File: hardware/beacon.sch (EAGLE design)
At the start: 13 parts, among them IC1 LM1117SX-3.3, IC2 FT232RL, X1 MINI-USB-UX60A-MB-5ST

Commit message: update schematic
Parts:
- added C5: 100n, rcl:C-EUC1206K
- added Q1, Q2: BC850SMD, transistor-npn:BC850SMD
- added R10, R4, R5, R6, R7, R8, R9: 10k, rcl:R-EU_R1206
- added RESET: (no value), switch-omron:10-XX
- added SV1: (no value), con-lstb:MA06-1
- added SV2: HC-SR04, con-lstb:MA04-1
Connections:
- new net DTR: IC2.!DTR, Q2.E, R4.1, SV1.6
- new net ECHO: SV2.2, U1.GPIO12
- new net GPIO0: Q2.C, R9.2, U1.GPIO0
- new net N$11: Q2.B, R5.2
- new net N$12: R10.2, U1.GPIO2
- new net N$6: R6.1, U1.GPIO15
- new net N$8: R7.2, U1.CH_PD
- new net N$9: Q1.B, R4.2
- new net RST: Q1.C, R8.2, RESET.S, RESET.S1, U1.RESET
- new net RTS: IC2.!RTS, Q1.E, R5.1
- new net TRIGGER: SV2.3, U1.GPIO13
- net +3V3: now also C5.1, R10.1, R7.1, R8.1, R9.1, SV1.3
- net +5V: now also SV2.4
- net GND: now also C5.2, R6.2, RESET.P, RESET.P1, SV1.1, SV2.1
- net RX: now also SV1.5
- net TX: now also SV1.4
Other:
- moved on the sheet: U1

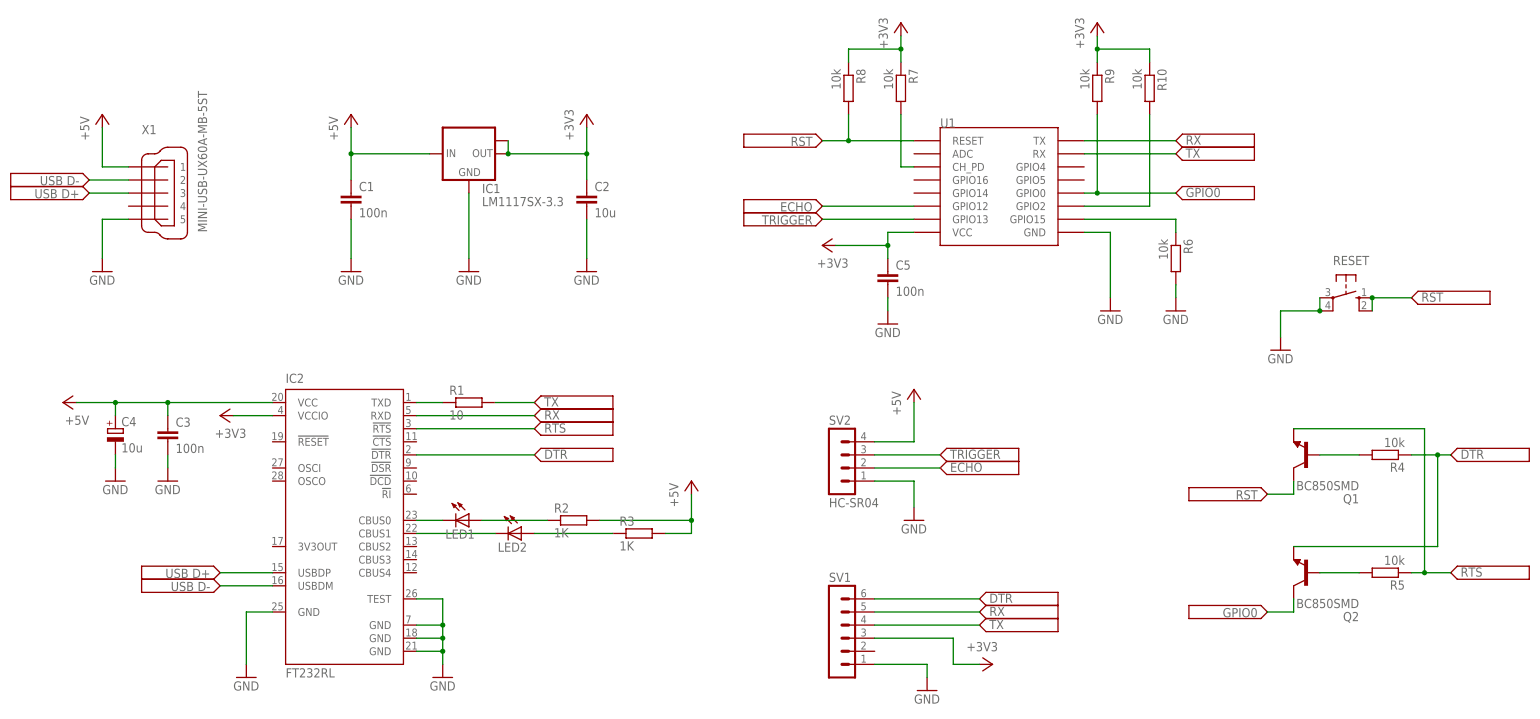
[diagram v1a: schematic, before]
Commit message: update schematic, change ft232 to ch340g
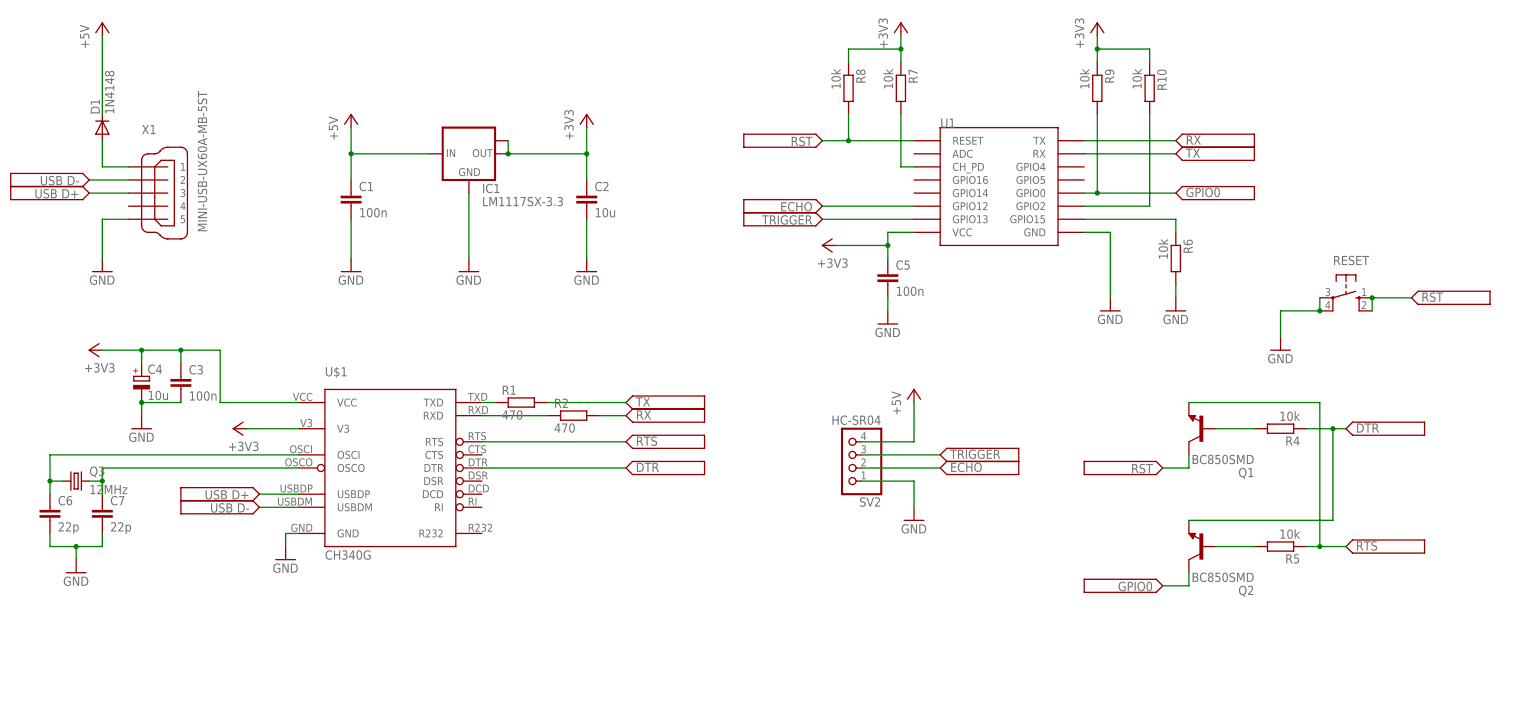
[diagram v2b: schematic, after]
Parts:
- removed IC2: FT232RL, ftdichip:FT232RL
- removed LED1, LED2: (no value), led:LEDSMT1206
- removed R3: 1K, rcl:R-EU_R1206
- removed SV1: (no value), con-lstb:MA06-1
- added C6, C7: 22p, rcl:C-EUC1206K
- added D1: 1N4148, diode:S1M
- added Q3: 12MHz, crystal:CRYSTALSM49
- added U$1: CH340G, ch340g:CH340G
- R1: value 10 -> 470
- R2: value 1K -> 470
- SV2: device con-lstb:MA04-1 -> pinhead:PINHD-1X4/90
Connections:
- net +3V3: now also C3.1, C4.+, U$1.V3, U$1.VCC; no longer IC2.VCCIO, SV1.3
- net +5V: now also D1.C; no longer C3.1, C4.+, IC2.VCC, R2.2, R3.2, X1.1
- net DTR: now also U$1.DTR; no longer IC2.!DTR, SV1.6
- net GND: now also C6.2, C7.2, U$1.GND; no longer IC2.GND, IC2.GND@1, IC2.GND@2, IC2.GND@A, IC2.TEST, SV1.1
- net N$1: now also R1.1, U$1.TXD; no longer IC2.CBUS0, LED1.C
- net N$2: now also R2.1, U$1.RXD; no longer IC2.CBUS1, LED2.C
- net N$3: now also C6.1, Q3.1, U$1.OSCI; no longer IC2.TXD, R1.1
- net N$4: now also C7.1, Q3.2, U$1.OSCO; no longer LED1.A, R2.1
- net N$5: now also D1.A, X1.1; no longer LED2.A, R3.1
- net RTS: now also U$1.RTS; no longer IC2.!RTS
- net RX: now also R2.2; no longer IC2.RXD, SV1.5
- net TX: no longer SV1.4
- net USBDM: now also U$1.USBDM; no longer IC2.USBDM
- net USBDP: now also U$1.USBDP; no longer IC2.USBDP
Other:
- moved on the sheet: C3, C4, Q1, Q2, R1, R2, R4, R5

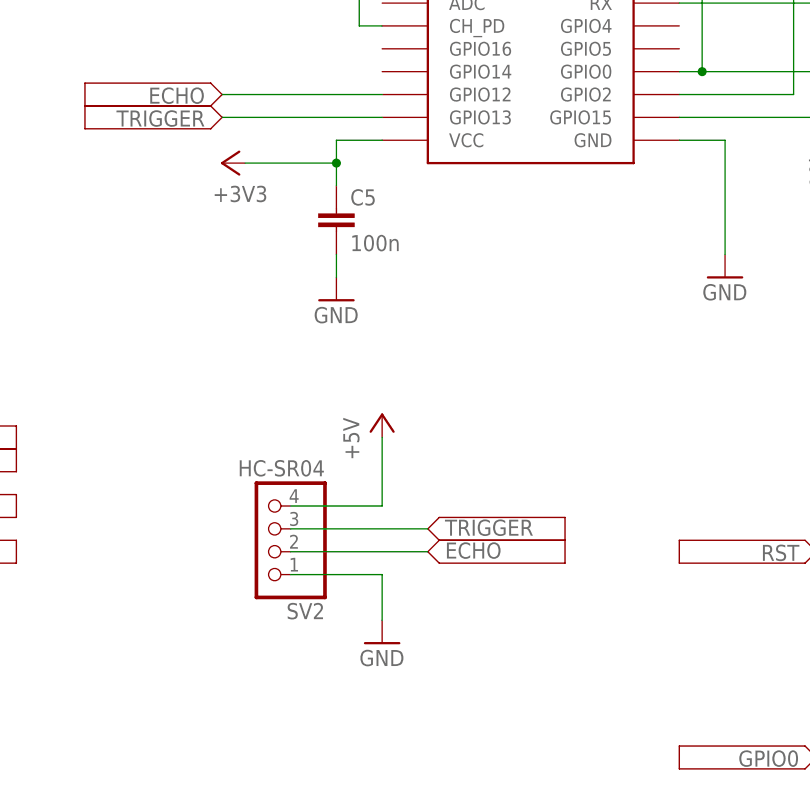
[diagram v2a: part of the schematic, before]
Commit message: create board, update ch340g lbr
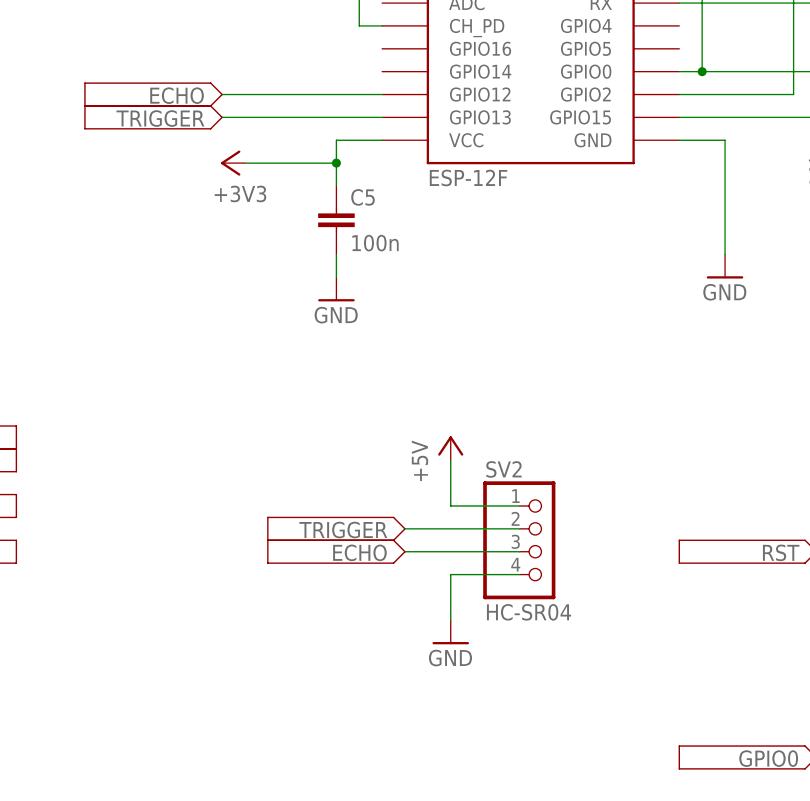
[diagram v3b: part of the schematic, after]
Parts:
- U1: value (none) -> ESP-12F
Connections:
- net +5V: now also SV2.1; no longer SV2.4
- net ECHO: now also SV2.3; no longer SV2.2
- net GND: now also SV2.4; no longer SV2.1
- net TRIGGER: now also SV2.2; no longer SV2.3
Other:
- moved on the sheet: SV2
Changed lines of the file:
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@@
 <parts>
 <part name="X1" library="con-hirose" deviceset="MINI-USB-" device="UX60A-MB-5ST"/>
-<part name="U1" library="esp8266modules" deviceset="ESP12" device="SMD"/>
+<part name="U1" library="esp8266modules" deviceset="ESP12" device="SMD" value="ESP-12F"/>
 <part name="IC1" library="lm1117" deviceset="LM1117SX-*" device="" technology="3.3"/>
 <part name="C1" library="rcl" deviceset="C-EU" device="C1206K" value="100n"/>
@@
 <instance part="GND13" gate="1" x="185.42" y="43.18"/>
 <instance part="+3V7" gate="G$1" x="170.18" y="99.06"/>
-<instance part="SV2" gate="A" x="121.92" y="15.24" rot="R180"/>
-<instance part="TRIGGER" gate="G$1" x="154.94" y="15.24"/>
-<instance part="ECHO" gate="G$1" x="154.94" y="12.7"/>
-<instance part="GND14" gate="1" x="134.62" y="2.54"/>
-<instance part="P+5" gate="1" x="134.62" y="27.94"/>
+<instance part="SV2" gate="A" x="152.4" y="12.7"/>
+<instance part="TRIGGER" gate="G$1" x="121.92" y="15.24" rot="R180"/>
+<instance part="ECHO" gate="G$1" x="121.92" y="12.7" rot="R180"/>
+<instance part="GND14" gate="1" x="142.24" y="2.54"/>
+<instance part="P+5" gate="1" x="142.24" y="25.4"/>
 <instance part="TRIGGER1" gate="G$1" x="101.6" y="60.96" rot="R180"/>
 <instance part="ECHO1" gate="G$1" x="101.6" y="63.5" rot="R180"/>
@@
 </segment>
 <segment>
-<pinref part="SV2" gate="A" pin="1"/>
-<pinref part="GND14" gate="1" pin="GND"/>
-<wire x1="124.46" y1="10.16" x2="134.62" y2="10.16" width="0.1524" layer="91"/>
-<wire x1="134.62" y1="10.16" x2="134.62" y2="5.08" width="0.1524" layer="91"/>
-</segment>
-<segment>
 <pinref part="R6" gate="G$1" pin="2"/>
 <pinref part="GND13" gate="1" pin="GND"/>
@@
 <wire x1="15.24" y1="0" x2="12.7" y2="0" width="0.1524" layer="91"/>
 <wire x1="12.7" y1="0" x2="12.7" y2="-2.54" width="0.1524" layer="91"/>
+</segment>
+<segment>
+<pinref part="SV2" gate="A" pin="4"/>
+<pinref part="GND14" gate="1" pin="GND"/>
+<wire x1="149.86" y1="10.16" x2="142.24" y2="10.16" width="0.1524" layer="91"/>
+<wire x1="142.24" y1="10.16" x2="142.24" y2="5.08" width="0.1524" layer="91"/>
 </segment>
 </net>
@@
 </segment>
 <segment>
-<pinref part="P+5" gate="1" pin="+5V"/>
-<pinref part="SV2" gate="A" pin="4"/>
-<wire x1="134.62" y1="25.4" x2="134.62" y2="17.78" width="0.1524" layer="91"/>
-<wire x1="134.62" y1="17.78" x2="124.46" y2="17.78" width="0.1524" layer="91"/>
-</segment>
-<segment>
 <pinref part="D1" gate="G$1" pin="C"/>
 <pinref part="P+2" gate="1" pin="+5V"/>
 <wire x1="-22.86" y1="81.28" x2="-22.86" y2="96.52" width="0.1524" layer="91"/>
 </segment>
+<segment>
+<pinref part="SV2" gate="A" pin="1"/>
+<pinref part="P+5" gate="1" pin="+5V"/>
+<wire x1="149.86" y1="17.78" x2="142.24" y2="17.78" width="0.1524" layer="91"/>
+<wire x1="142.24" y1="17.78" x2="142.24" y2="22.86" width="0.1524" layer="91"/>
+</segment>
 </net>
 <net name="USBDP" class="0">
@@
 <net name="TRIGGER" class="0">
 <segment>
-<pinref part="SV2" gate="A" pin="3"/>
-<wire x1="139.7" y1="15.24" x2="124.46" y2="15.24" width="0.1524" layer="91"/>
-</segment>
-<segment>
 <pinref part="U1" gate="G$1" pin="GPIO13"/>
 <wire x1="134.62" y1="60.96" x2="116.84" y2="60.96" width="0.1524" layer="91"/>
 </segment>
+<segment>
+<pinref part="SV2" gate="A" pin="2"/>
+<wire x1="149.86" y1="15.24" x2="137.16" y2="15.24" width="0.1524" layer="91"/>
+</segment>
 </net>
 <net name="ECHO" class="0">
-<segment>
-<pinref part="SV2" gate="A" pin="2"/>
-<wire x1="139.7" y1="12.7" x2="124.46" y2="12.7" width="0.1524" layer="91"/>
-</segment>
 <segment>
 <pinref part="U1" gate="G$1" pin="GPIO12"/>
 <wire x1="134.62" y1="63.5" x2="116.84" y2="63.5" width="0.1524" layer="91"/>
+</segment>
+<segment>
+<pinref part="SV2" gate="A" pin="3"/>
+<wire x1="149.86" y1="12.7" x2="137.16" y2="12.7" width="0.1524" layer="91"/>
 </segment>
 </net>
@@
 </sheet>
 </sheets>
+<errors>
+</errors>
 </schematic>
 </drawing>

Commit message: add test pads
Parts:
- added TP1, TP2, TP3, TP4: TPSQTP20SQ, testpad:TPSQTP20SQ
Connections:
- net +3V3: now also TP4.TP
- net GND: now also TP1.TP
- net RX: now also TP3.TP
- net TX: now also TP2.TP
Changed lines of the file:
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@@
 <part name="GND8" library="supply1" deviceset="GND" device=""/>
 <part name="D1" library="diode" deviceset="S1M" device="" value="1N4148"/>
+<part name="TP1" library="testpad" deviceset="TPSQ" device="TP20SQ"/>
+<part name="TP2" library="testpad" deviceset="TPSQ" device="TP20SQ"/>
+<part name="TP3" library="testpad" deviceset="TPSQ" device="TP20SQ"/>
+<part name="GND9" library="supply1" deviceset="GND" device=""/>
+<part name="TX2" library="supply2" deviceset="V&lt;--" device="" value="TX"/>
+<part name="RX2" library="supply2" deviceset="V&lt;--" device="" value="RX"/>
+<part name="TP4" library="testpad" deviceset="TPSQ" device="TP20SQ"/>
+<part name="+3V4" library="supply1" deviceset="+3V3" device=""/>
 </parts>
 <sheets>
@@
 <instance part="GND8" gate="1" x="-27.94" y="-7.62"/>
 <instance part="D1" gate="G$1" x="-22.86" y="78.74" rot="R90"/>
+<instance part="TP1" gate="G$1" x="220.98" y="66.04" rot="R270"/>
+<instance part="TP2" gate="G$1" x="220.98" y="71.12" rot="R270"/>
+<instance part="TP3" gate="G$1" x="220.98" y="76.2" rot="R270"/>
+<instance part="GND9" gate="1" x="228.6" y="60.96"/>
+<instance part="TX2" gate="G$1" x="248.92" y="71.12"/>
+<instance part="RX2" gate="G$1" x="248.92" y="76.2"/>
+<instance part="TP4" gate="G$1" x="220.98" y="81.28" rot="R270"/>
+<instance part="+3V4" gate="G$1" x="228.6" y="88.9"/>
 </instances>
 <busses>
@@
 <wire x1="149.86" y1="10.16" x2="142.24" y2="10.16" width="0.1524" layer="91"/>
 <wire x1="142.24" y1="10.16" x2="142.24" y2="5.08" width="0.1524" layer="91"/>
+</segment>
+<segment>
+<pinref part="TP1" gate="G$1" pin="TP"/>
+<pinref part="GND9" gate="1" pin="GND"/>
+<wire x1="223.52" y1="66.04" x2="228.6" y2="66.04" width="0.1524" layer="91"/>
+<wire x1="228.6" y1="66.04" x2="228.6" y2="63.5" width="0.1524" layer="91"/>
 </segment>
 </net>
@@
 <wire x1="0" y1="25.4" x2="0" y2="35.56" width="0.1524" layer="91"/>
 </segment>
+<segment>
+<pinref part="TP4" gate="G$1" pin="TP"/>
+<pinref part="+3V4" gate="G$1" pin="+3V3"/>
+<wire x1="223.52" y1="81.28" x2="228.6" y2="81.28" width="0.1524" layer="91"/>
+<wire x1="228.6" y1="81.28" x2="228.6" y2="86.36" width="0.1524" layer="91"/>
+</segment>
 </net>
 <net name="+5V" class="0">
@@
 <wire x1="73.66" y1="22.86" x2="78.74" y2="22.86" width="0.1524" layer="91"/>
 </segment>
+<segment>
+<pinref part="TP3" gate="G$1" pin="TP"/>
+<wire x1="223.52" y1="76.2" x2="233.68" y2="76.2" width="0.1524" layer="91"/>
+</segment>
 </net>
 <net name="TX" class="0">
@@
 <wire x1="63.5" y1="25.4" x2="78.74" y2="25.4" width="0.1524" layer="91"/>
 </segment>
-</net>
+<segment>
+<pinref part="TP2" gate="G$1" pin="TP"/>
+<wire x1="233.68" y1="71.12" x2="223.52" y2="71.12" width="0.1524" layer="91"/>
+</segment>
+</net>
